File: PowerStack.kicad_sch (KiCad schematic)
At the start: 36 parts, among them P7 Solder Pad, U4 DRV8300D

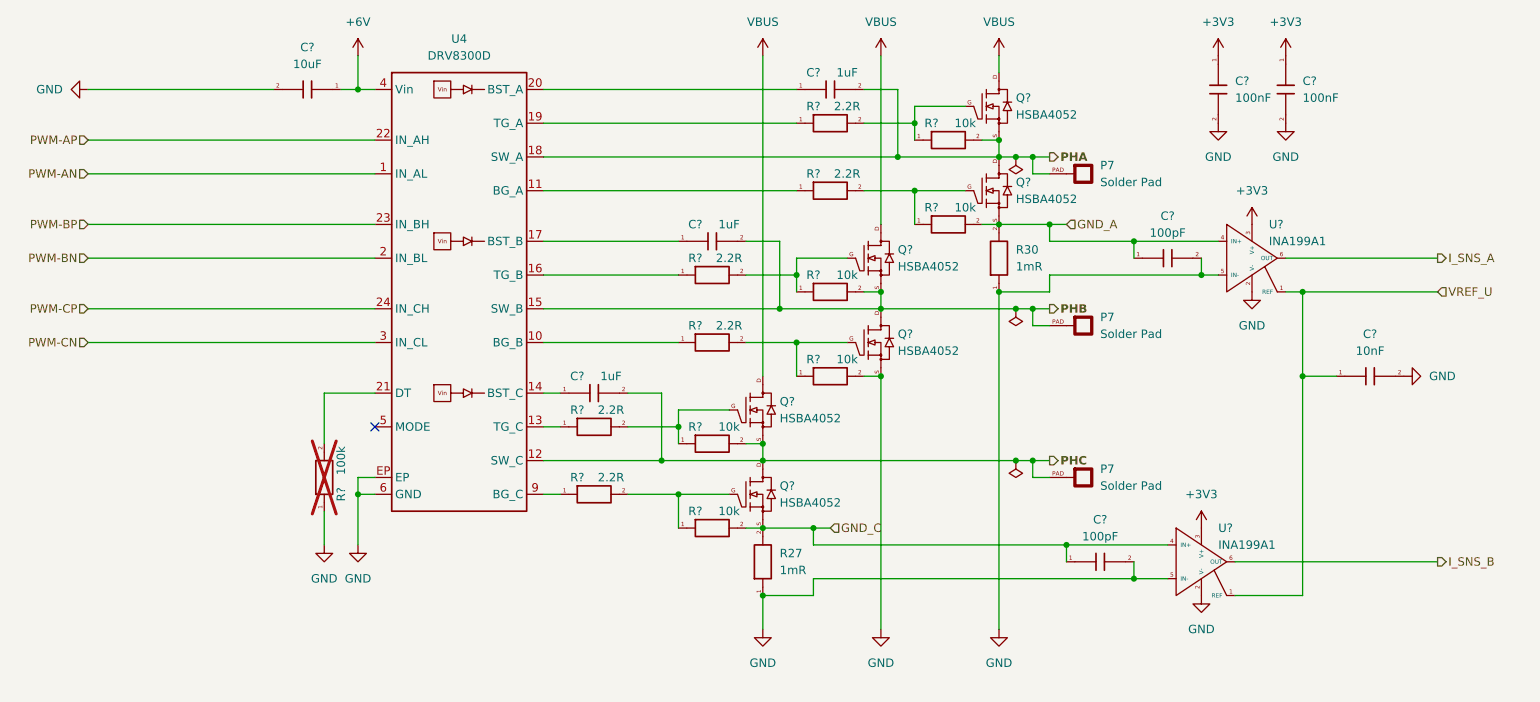
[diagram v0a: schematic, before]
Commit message: Update layout and modified sense amplifier
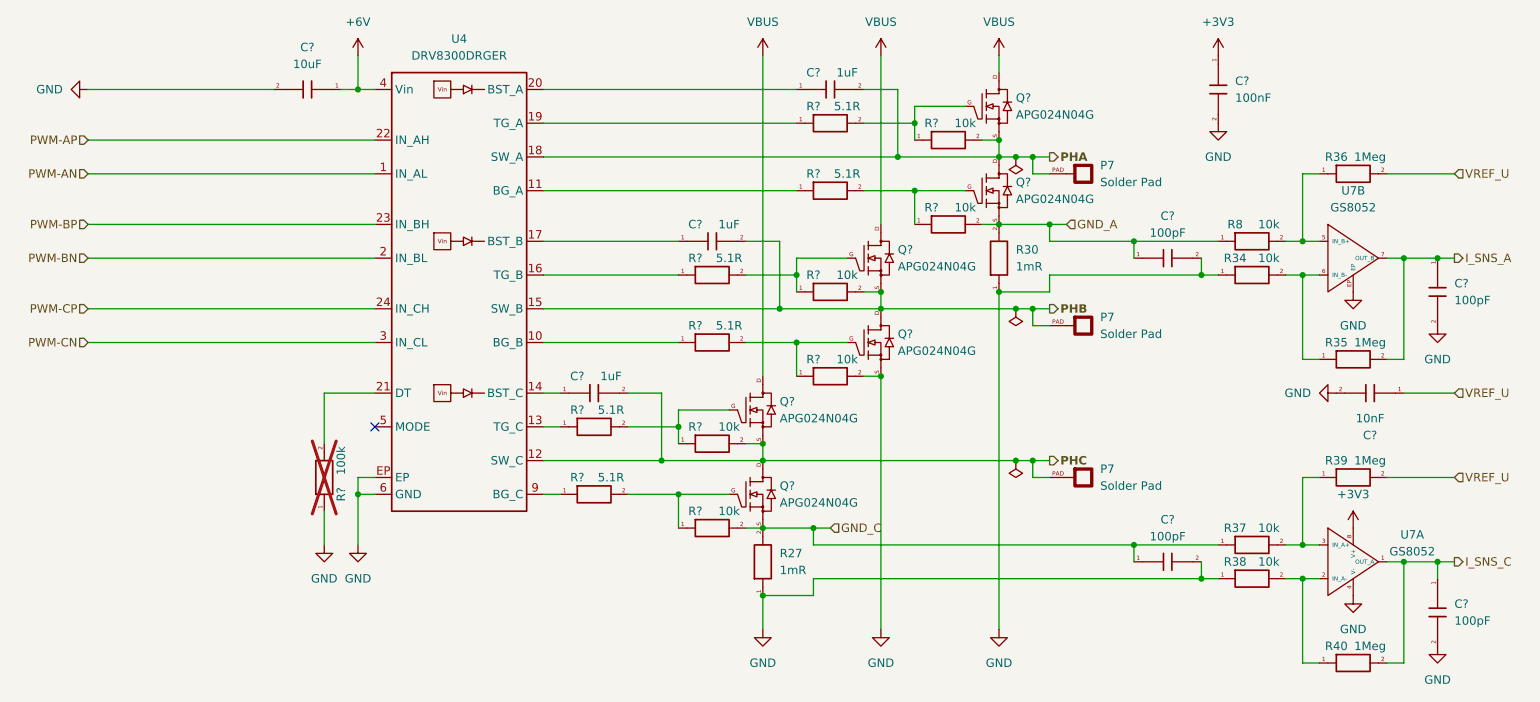
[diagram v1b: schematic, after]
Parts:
- removed C?: 100nF, 001_GN_RCL_SMD:C0201(0603M), symbol 001_Basic_PassiveComponents:101_Capacitor
- removed U? (x2): INA199A1, 003_GN_SMALL-SEMI_SMD:SOT-363, symbol 101_IntegratedCircuit_Amplifier:INA199A1
- added C? (x2): 100pF, 001_GN_RCL_SMD:C0201(0603M), symbol 001_Basic_PassiveComponents:101_Capacitor
- added R34, R37, R38, R8: 10k, 001_GN_RCL_SMD:R0201(0603M), symbol 001_Basic_PassiveComponents:001_Resistor
- added R35, R36, R39, R40: 1Meg, 001_GN_RCL_SMD:R0201(0603M), symbol 001_Basic_PassiveComponents:001_Resistor
- added U7: GS8052, 003_GN_SMALL-SEMI_SMD:DFN-8_2020, symbol 101_IntegratedCircuit_Amplifier:GS8052-FR
- Q? (x6): value HSBA4052 -> APG024N04G
- R? (x6): value 2.2R -> 5.1R
- R?: now in the parts list
- U4: value DRV8300D -> DRV8300DRGER
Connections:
- net +3V3: now also U7.8 (V+)
- net GND: now also C?.2, C?.2, R34.1, R38.1, U7.4 (V-), U7.EP
- net GND_A: now also R8.1
- net GND_C: now also R37.1
- net I_SNS_A: now also C?.1, R35.2, U7.7 (OUT_B)
- net VREF_U: now also R36.2, R39.2
- new net: R34.2, R35.1, U7.6 (IN_B-)
- new net: R37.2, R39.1, U7.3 (IN_A+)
- new net: R38.2, R40.1, U7.2 (IN_A-)
- new net: R36.1, R8.2, U7.5 (IN_B+)
- new net I_SNS_C: C?.1, R40.2, U7.1 (OUT_A)
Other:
- moved on the sheet: C?

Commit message: Modified the scheme of current sensing
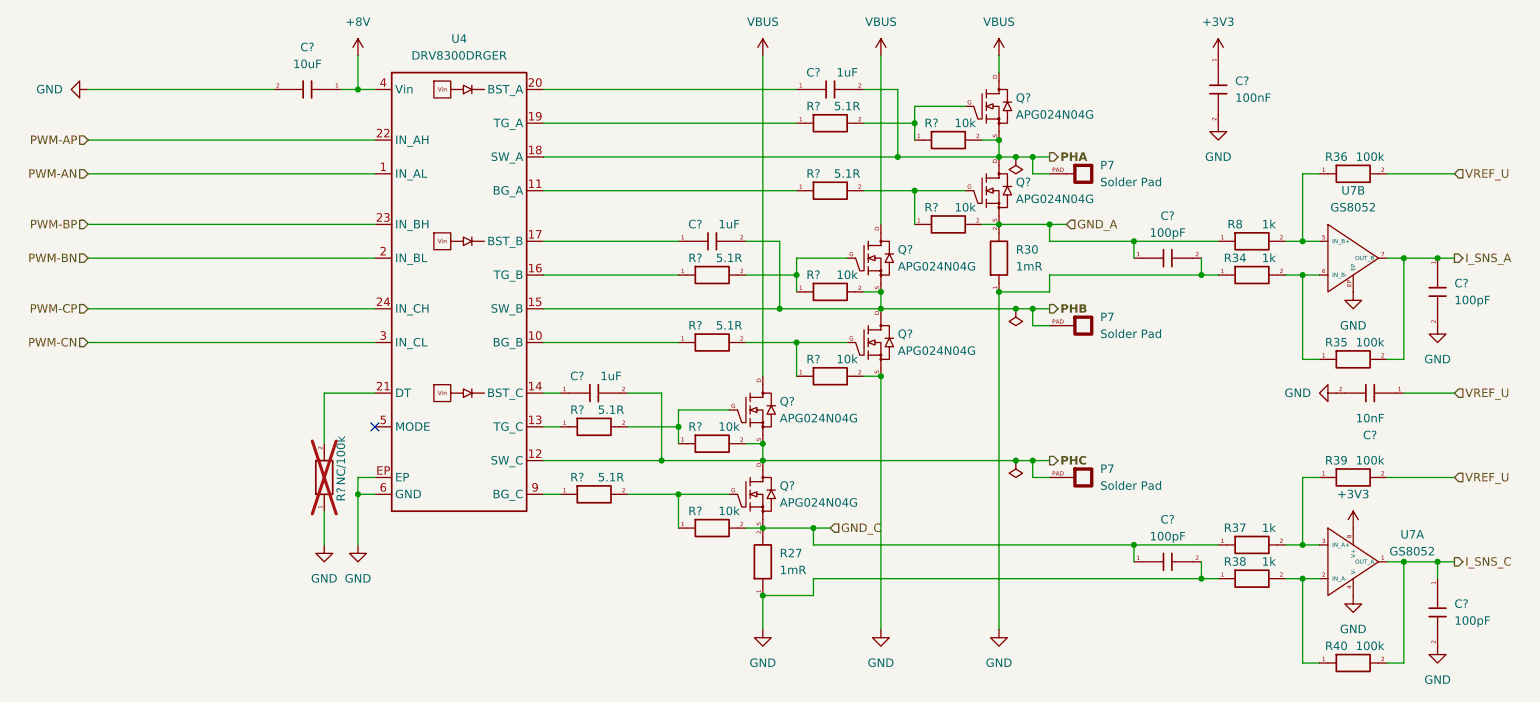
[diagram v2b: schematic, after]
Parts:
- P7: now left out of the parts list
- R34, R37, R38, R8: value 10k -> 1k
- R35, R36, R39, R40: value 1Meg -> 100k
- R?: value 100k -> NC/100k
- U4: Symbol type (none) -> Specified Device
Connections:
- net +6V renamed +8V
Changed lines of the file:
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@@
       (effects (font (size 1.27 1.27)))
     )
-    (property "Value" "10k" (at 223.52 96.52 0)
+    (property "Value" "1k" (at 223.52 96.52 0)
       (effects (font (size 1.27 1.27)))
     )
@@
       (effects (font (size 1.27 1.27)))
     )
-    (property "Value" "1Meg" (at 238.76 127 0)
+    (property "Value" "100k" (at 238.76 127 0)
       (effects (font (size 1.27 1.27)))
     )
@@
       (effects (font (size 1.27 1.27)))
     )
-    (property "Value" "1Meg" (at 238.76 81.28 0)
+    (property "Value" "100k" (at 238.76 81.28 0)
       (effects (font (size 1.27 1.27)))
     )
@@
   )
   (symbol (lib_id "301_Link_Pad:Pad_Square") (at 195.58 129.54 0) (unit 1)
-    (in_bom yes) (on_board yes) (dnp no) (fields_autoplaced)
+    (in_bom no) (on_board yes) (dnp no) (fields_autoplaced)
     (property "Reference" "P7" (at 198.12 128.27 0)
       (effects (font (size 1.27 1.27)) (justify left))
@@
       (effects (font (size 1.27 1.27)))
     )
-    (property "Value" "1Meg" (at 238.76 109.22 0)
+    (property "Value" "100k" (at 238.76 109.22 0)
       (effects (font (size 1.27 1.27)))
     )
@@
       (effects (font (size 1.27 1.27)))
     )
-    (property "Value" "10k" (at 223.52 137.16 0)
+    (property "Value" "1k" (at 223.52 137.16 0)
       (effects (font (size 1.27 1.27)))
     )
@@
       (effects (font (size 1.27 1.27)))
     )
-    (property "Value" "10k" (at 223.52 91.44 0)
+    (property "Value" "1k" (at 223.52 91.44 0)
       (effects (font (size 1.27 1.27)))
     )
@@
   )
   (symbol (lib_id "301_Link_Pad:Pad_Square") (at 195.58 106.68 0) (unit 1)
-    (in_bom yes) (on_board yes) (dnp no) (fields_autoplaced)
+    (in_bom no) (on_board yes) (dnp no) (fields_autoplaced)
     (property "Reference" "P7" (at 198.12 105.41 0)
       (effects (font (size 1.27 1.27)) (justify left))
@@
       (effects (font (size 1.27 1.27)))
     )
-    (property "Value" "10k" (at 223.52 142.24 0)
+    (property "Value" "1k" (at 223.52 142.24 0)
       (effects (font (size 1.27 1.27)))
     )
@@
       (effects (font (size 1.27 1.27)))
     )
-    (property "Value" "1Meg" (at 238.76 154.94 0)
+    (property "Value" "100k" (at 238.76 154.94 0)
       (effects (font (size 1.27 1.27)))
     )
@@
     )
     (property "Datasheet" "" (at 96.52 109.22 0)
+      (effects (font (size 1.27 1.27)) hide)
+    )
+    (property "Symbol type" "Specified Device" (at 101.6 101.6 0)
       (effects (font (size 1.27 1.27)) hide)
     )
@@
   )
   (symbol (lib_id "301_Link_Pad:Pad_Square") (at 195.58 83.82 0) (unit 1)
-    (in_bom yes) (on_board yes) (dnp no) (fields_autoplaced)
+    (in_bom no) (on_board yes) (dnp no) (fields_autoplaced)
     (property "Reference" "P7" (at 198.12 82.55 0)
       (effects (font (size 1.27 1.27)) (justify left))
@@
     )
   )
-  (symbol (lib_id "PowerPort:+6V") (at 86.36 66.04 0) (unit 1)
+  (symbol (lib_id "PowerPort:+8V") (at 86.36 66.04 0) (unit 1)
     (in_bom yes) (on_board yes) (dnp no) (fields_autoplaced)
     (property "Reference" "#PWR067" (at 86.36 69.85 0)
       (effects (font (size 1.27 1.27)) hide)
     )
-    (property "Value" "+6V" (at 86.36 60.96 0)
+    (property "Value" "+8V" (at 86.36 60.96 0)
       (effects (font (size 1.27 1.27)))
     )
@@
         )
         (path "/890f51e2-19fc-47da-b01c-61fe647223a1/31fa03ea-a281-4b4a-87b0-e26cab6bc242"
-          (reference "#PWR080") (unit 1)
+          (reference "#PWR?") (unit 1)
         )
       )
@@
       (effects (font (size 1.27 1.27)))
     )
-    (property "Value" "100k" (at 83.82 127 0)
-      (effects (font (size 1.27 1.27)))
-    )
+    (property "Value" "NC/100k" (at 83.82 127 0)
+      (effects (font (size 1.27 1.27)))
+    )
